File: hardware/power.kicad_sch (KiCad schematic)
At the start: 0 parts

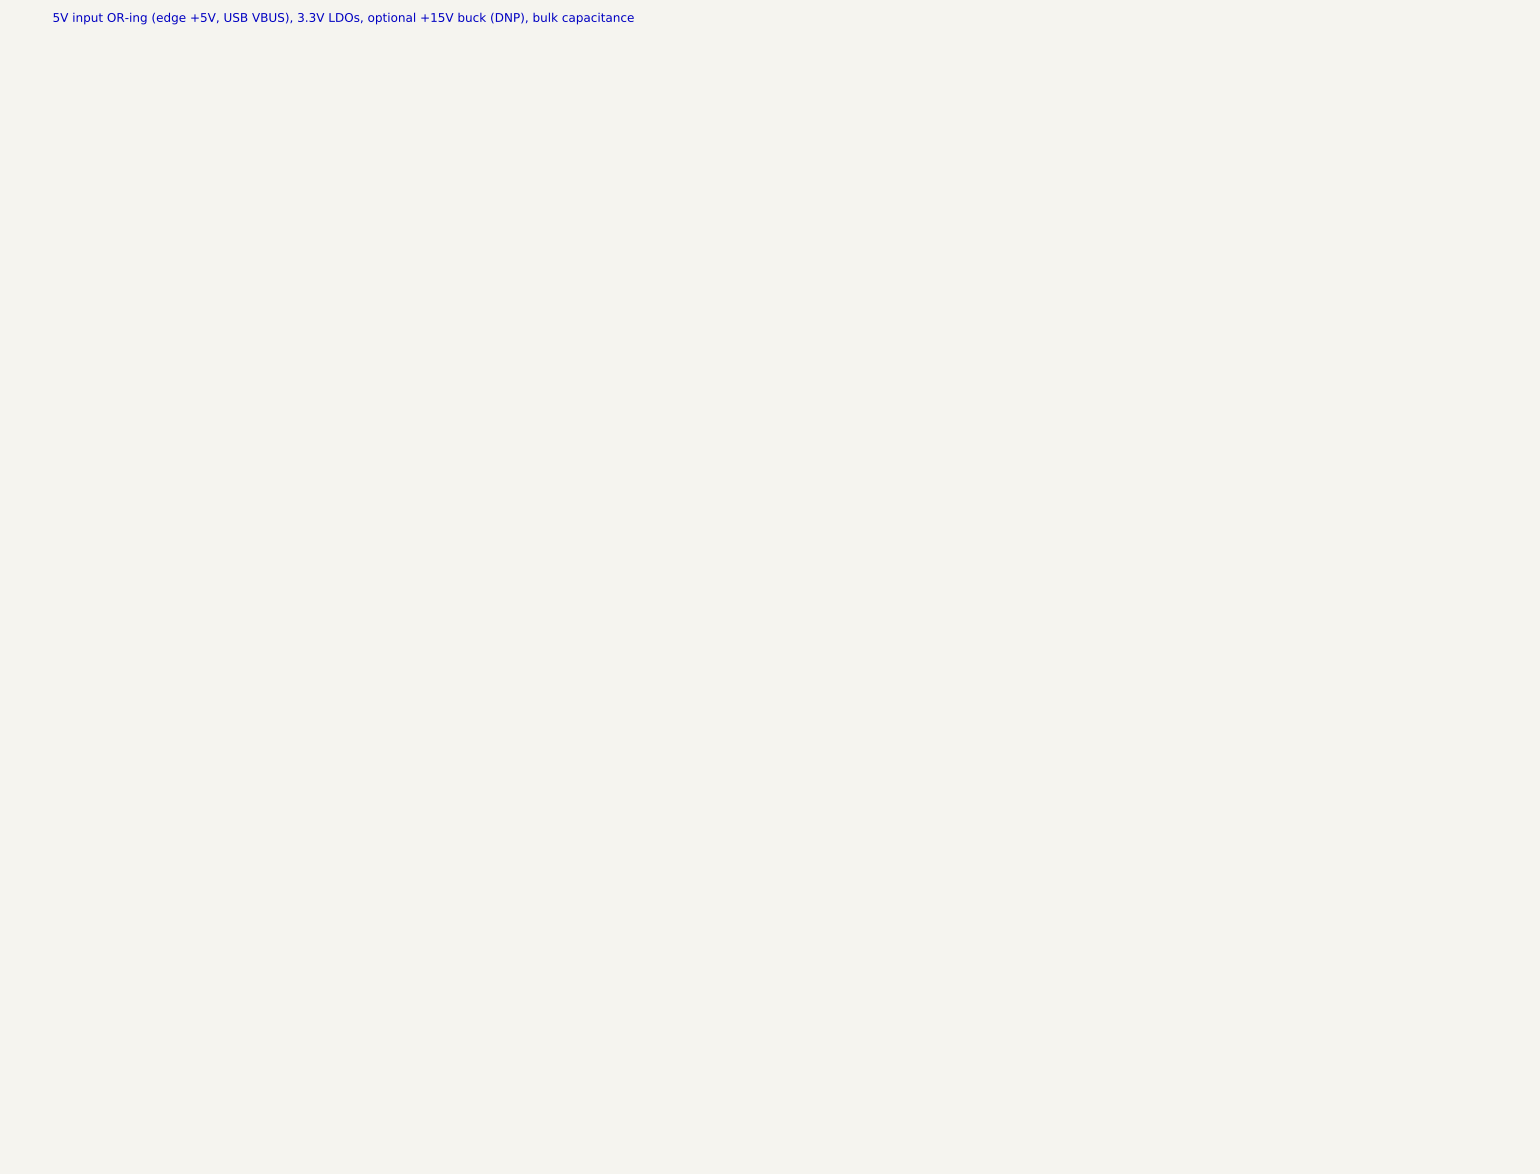
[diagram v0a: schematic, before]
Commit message: Remaining sheets: power, SD and display, WiFi, audio, joystick; ERC clean
- Power: Schottky diode-OR of edge +5V and USB VBUS (card runs from the
  2068/expansion bus, USB alone, or both), two TLV1117LV33 LDOs, bulk caps
- SD: Hirose DM3AT in SPI mode with series R, pull-ups, card detect to STAT
- OLED: 7-pin header (Waveshare 1.27in 128x96 SSD1351) on SPI1
- WiFi: ESP32-C3-WROOM-02 on UART, EN/boot from CTL, IO8 pull-up
- Audio: PWM low-pass, 2068 SOUND mix, MCP6002 buffers, 3.5 mm jack
- Joystick: DE-9 Kempston with pull-ups, series R, optional +5V jumper
- Memory sheet: activity LED on CTL bit 6
- Docs: power decision updated

Co-Authored-By: Claude Fable 5.1 <noreply@anthropic.com>
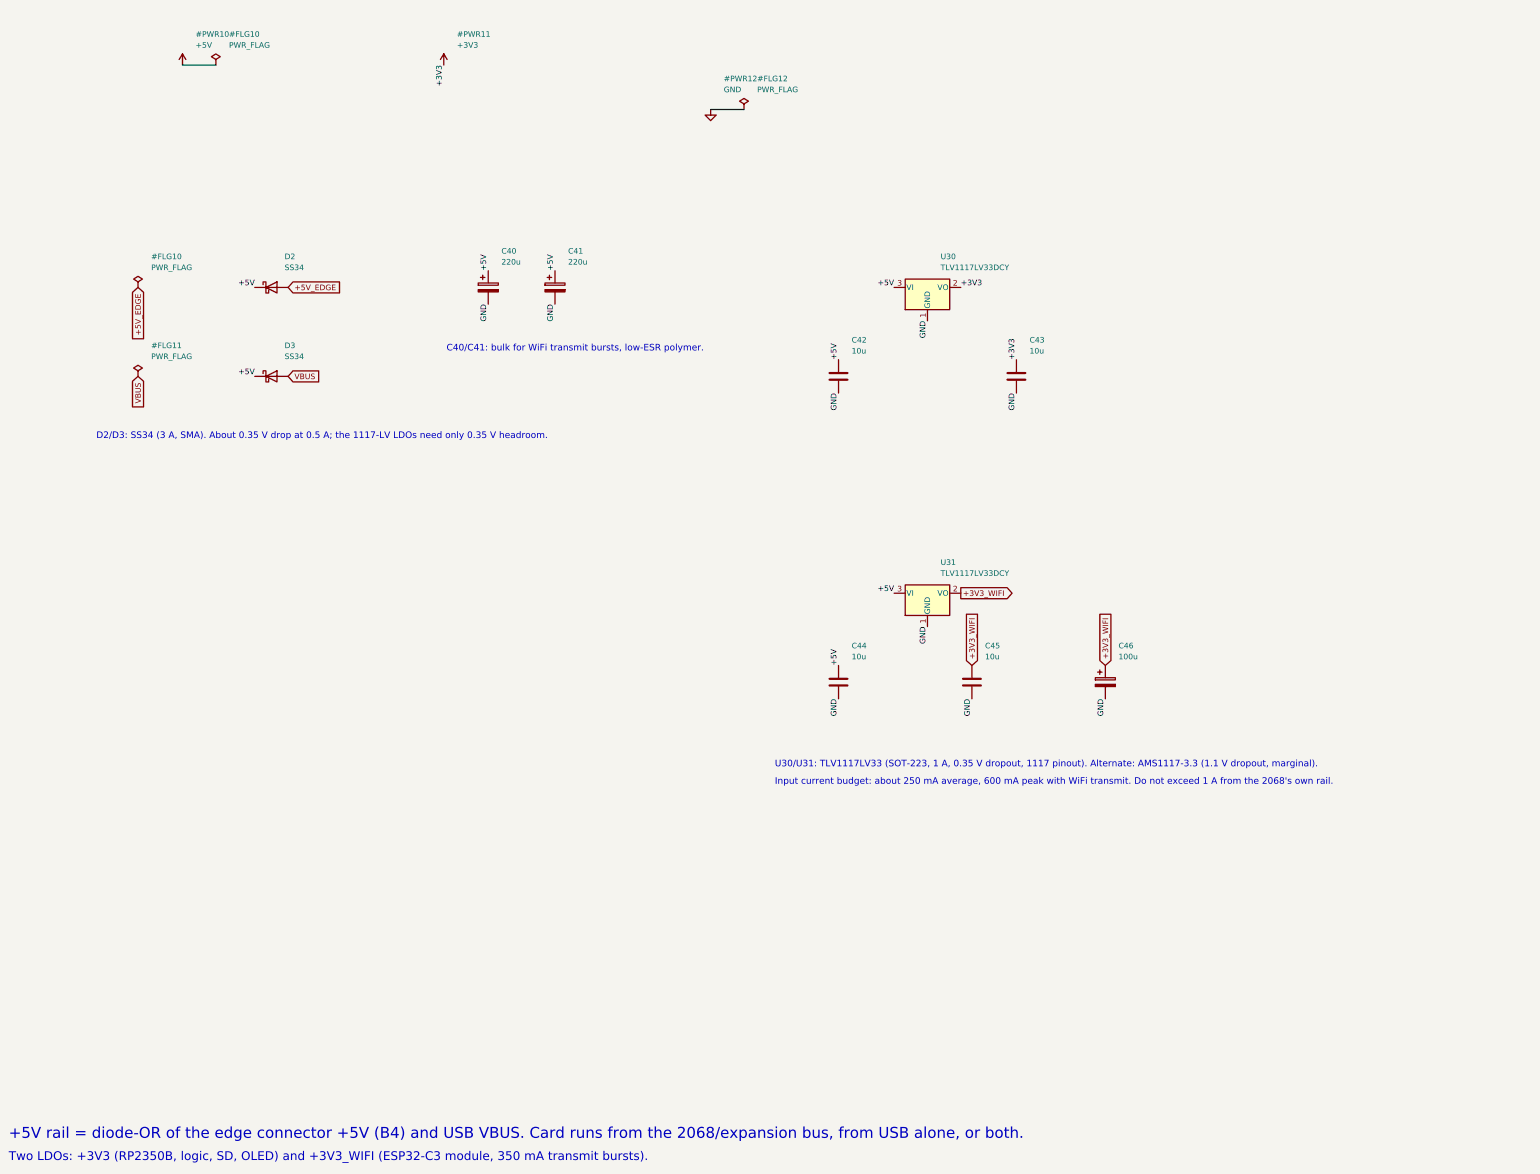
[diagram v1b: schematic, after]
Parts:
- added C40, C41: 220u, Capacitor_SMD:CP_Elec_6.3x7.7, symbol Device:C_Polarized
- added C42, C43, C44, C45: 10u, Capacitor_SMD:C_0805_2012Metric, symbol Device:C
- added C46: 100u, Capacitor_SMD:CP_Elec_6.3x7.7, symbol Device:C_Polarized
- added D2, D3: SS34, Diode_SMD:D_SMA, symbol Device:D_Schottky
- added U30, U31: TLV1117LV33DCY, Package_TO_SOT_SMD:SOT-223-3_TabPin2, symbol Regulator_Linear:TLV1117-33
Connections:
- new net +3V3: C43.1, U30.2 (VO)
- new net +3V3_WIFI: C45.1, C46.1, U31.2 (VO)
- new net +5V: C40.1, C41.1, C42.1, C44.1, D2.1 (K), D3.1 (K), U30.3 (VI), U31.3 (VI)
- new net +5V_EDGE: D2.2 (A)
- new net GND: C40.2, C41.2, C42.2, C43.2, C44.2, C45.2, C46.2, U30.1 (GND), U31.1 (GND)
- new net VBUS: D3.2 (A)
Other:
- note added: "+5V rail = diode-OR of the edge connector +5V (B4) and USB VBUS. Card runs from the 2068/expansion bus, from USB alone, or both."
- note added: "C40/C41: bulk for WiFi transmit bursts, low-ESR polymer."
- note added: "D2/D3: SS34 (3 A, SMA). About 0.35 V drop at 0.5 A; the 1117-LV LDOs need only 0.35 V headroom."
- note added: "Input current budget: about 250 mA average, 600 mA peak with WiFi transmit. Do not exceed 1 A from the 2068's own rail."
- note added: "Two LDOs: +3V3 (RP2350B, logic, SD, OLED) and +3V3_WIFI (ESP32-C3 module, 350 mA transmit bursts)."
- note added: "U30/U31: TLV1117LV33 (SOT-223, 1 A, 0.35 V dropout, 1117 pinout). Alternate: AMS1117-3.3 (1.1 V dropout, marginal)."
- note removed: "5V input OR-ing (edge +5V, USB VBUS), 3.3V LDOs, optional +15V buck (DNP), bulk capacitance"

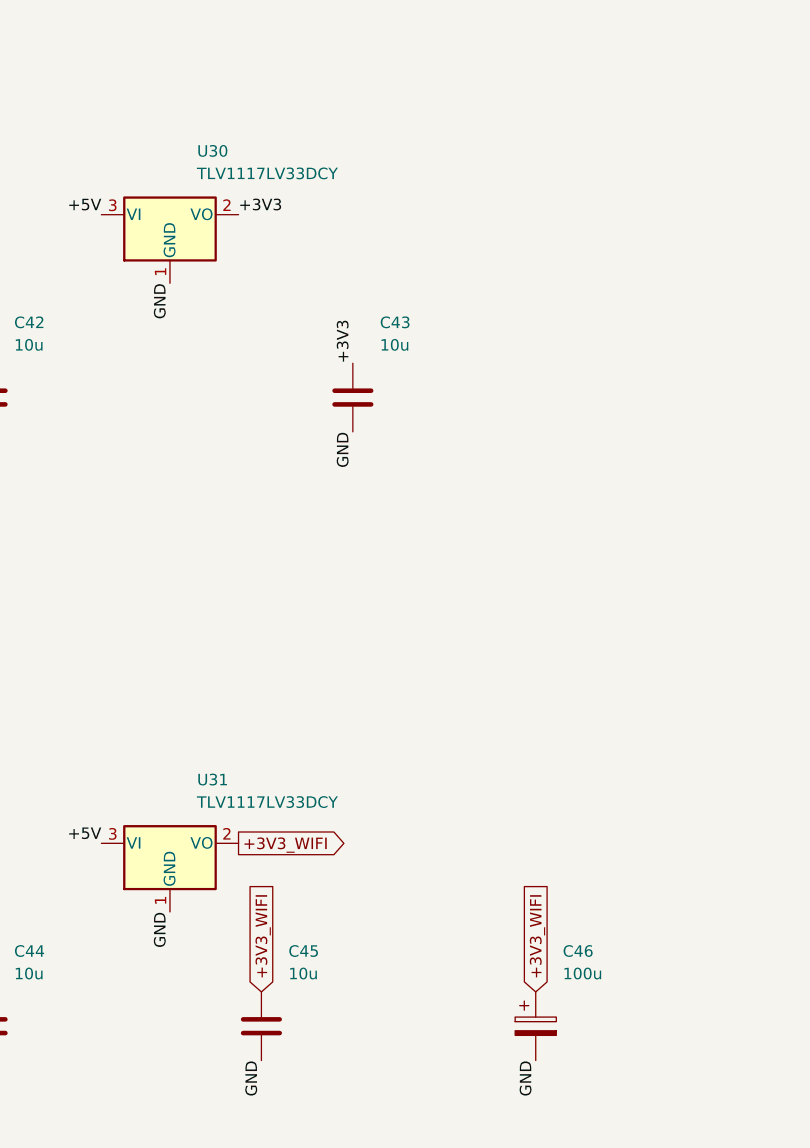
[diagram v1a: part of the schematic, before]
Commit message: BOM pass: LCSC and MPN fields on every part, JLCPCB BOM export
- scripts/parts.py: part table looked up 2026-09-16; schlib stamps fields
- substitutions for stock: 74HC273PW, 74LVC139PW, TI LVC04/08/126/574/1G86,
  33R USB series, XKB TS-1187A switches, Panasonic polymer 220uF, B5819W
- bom/: JLCPCB-format and full BOM CSVs

Co-Authored-By: Claude Fable 5.1 <noreply@anthropic.com>
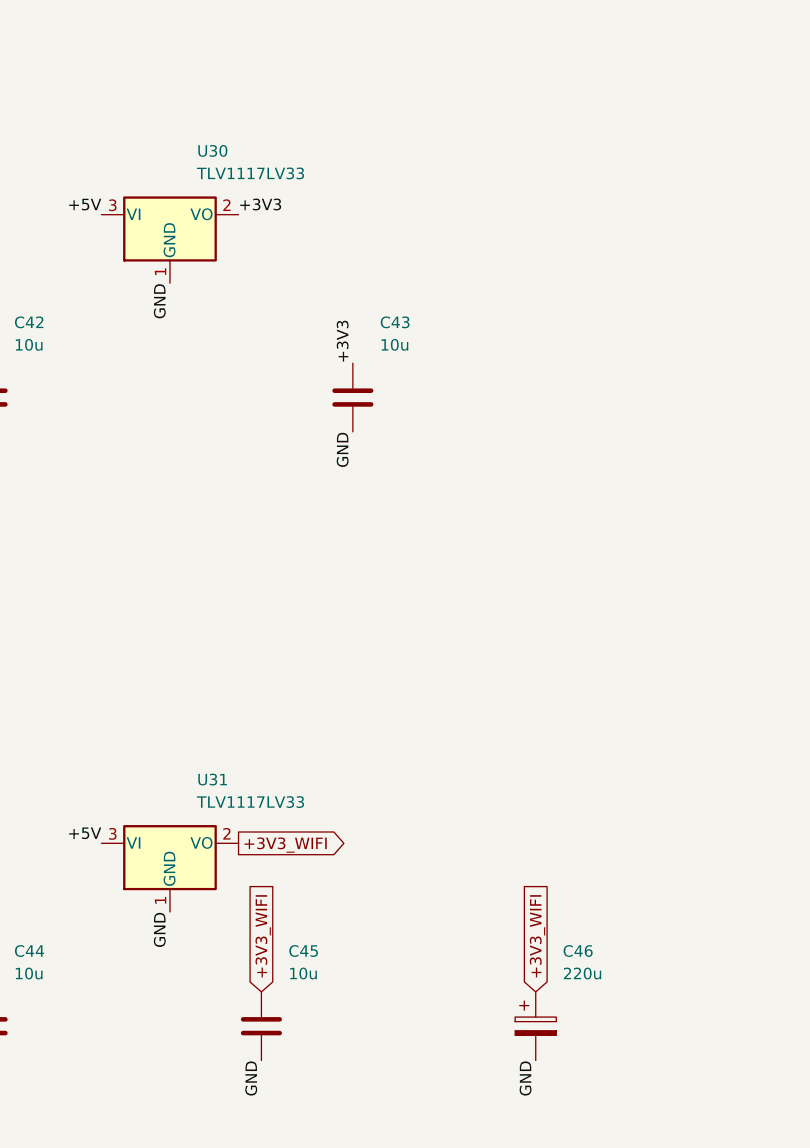
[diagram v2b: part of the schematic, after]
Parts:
- C40, C41: footprint Capacitor_SMD:CP_Elec_6.3x7.7 -> Capacitor_SMD:CP_Elec_6.3x5.9; LCSC (none) -> C128504; MPN (none) -> 6SVPC220MV
- C42, C43, C44, C45: LCSC (none) -> C15850; MPN (none) -> CL21A106KAYNNNE
- C46: value 100u -> 220u; footprint Capacitor_SMD:CP_Elec_6.3x7.7 -> Capacitor_SMD:CP_Elec_6.3x5.9; LCSC (none) -> C128504; MPN (none) -> 6SVPC220MV
- D2, D3: LCSC (none) -> C8678; MPN (none) -> SS34
- U30, U31: value TLV1117LV33DCY -> TLV1117LV33; LCSC (none) -> C15578; MPN (none) -> TLV1117LV33DCYR
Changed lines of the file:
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@@
     (property "Datasheet" "" (at 80.01 90.17 0) (effects (font (size 1.27 1.27)) (justify left) (hide yes)))
     (property "Description" "" (at 80.01 90.17 0) (effects (font (size 1.27 1.27)) (justify left) (hide yes)))
+    (property "MPN" "SS34" (at 80.01 90.17 0) (effects (font (size 1.27 1.27)) (justify left) (hide yes)))
+    (property "LCSC" "C8678" (at 80.01 90.17 0) (effects (font (size 1.27 1.27)) (justify left) (hide yes)))
     (pin "1")
     (pin "2")
@@
     (property "Datasheet" "" (at 80.01 110.49 0) (effects (font (size 1.27 1.27)) (justify left) (hide yes)))
     (property "Description" "" (at 80.01 110.49 0) (effects (font (size 1.27 1.27)) (justify left) (hide yes)))
+    (property "MPN" "SS34" (at 80.01 110.49 0) (effects (font (size 1.27 1.27)) (justify left) (hide yes)))
+    (property "LCSC" "C8678" (at 80.01 110.49 0) (effects (font (size 1.27 1.27)) (justify left) (hide yes)))
     (pin "1")
     (pin "2")
@@
     (property "Reference" "C40" (at 132.54 81.86 0) (effects (font (size 1.27 1.27)) (justify left)))
     (property "Value" "220u" (at 132.54 84.36 0) (effects (font (size 1.27 1.27)) (justify left)))
-    (property "Footprint" "Capacitor_SMD:CP_Elec_6.3x7.7" (at 129.54 90.17 0) (effects (font (size 1.27 1.27)) (justify left) (hide yes)))
+    (property "Footprint" "Capacitor_SMD:CP_Elec_6.3x5.9" (at 129.54 90.17 0) (effects (font (size 1.27 1.27)) (justify left) (hide yes)))
     (property "Datasheet" "" (at 129.54 90.17 0) (effects (font (size 1.27 1.27)) (justify left) (hide yes)))
     (property "Description" "" (at 129.54 90.17 0) (effects (font (size 1.27 1.27)) (justify left) (hide yes)))
+    (property "MPN" "6SVPC220MV" (at 129.54 90.17 0) (effects (font (size 1.27 1.27)) (justify left) (hide yes)))
+    (property "LCSC" "C128504" (at 129.54 90.17 0) (effects (font (size 1.27 1.27)) (justify left) (hide yes)))
     (pin "1")
     (pin "2")
@@
     (property "Reference" "C41" (at 147.78 81.86 0) (effects (font (size 1.27 1.27)) (justify left)))
     (property "Value" "220u" (at 147.78 84.36 0) (effects (font (size 1.27 1.27)) (justify left)))
-    (property "Footprint" "Capacitor_SMD:CP_Elec_6.3x7.7" (at 144.78 90.17 0) (effects (font (size 1.27 1.27)) (justify left) (hide yes)))
+    (property "Footprint" "Capacitor_SMD:CP_Elec_6.3x5.9" (at 144.78 90.17 0) (effects (font (size 1.27 1.27)) (justify left) (hide yes)))
     (property "Datasheet" "" (at 144.78 90.17 0) (effects (font (size 1.27 1.27)) (justify left) (hide yes)))
     (property "Description" "" (at 144.78 90.17 0) (effects (font (size 1.27 1.27)) (justify left) (hide yes)))
+    (property "MPN" "6SVPC220MV" (at 144.78 90.17 0) (effects (font (size 1.27 1.27)) (justify left) (hide yes)))
+    (property "LCSC" "C128504" (at 144.78 90.17 0) (effects (font (size 1.27 1.27)) (justify left) (hide yes)))
     (pin "1")
     (pin "2")
@@
     (exclude_from_sim no) (in_bom yes) (on_board yes) (dnp no)
     (property "Reference" "U30" (at 232.87 83.13 0) (effects (font (size 1.27 1.27)) (justify left)))
-    (property "Value" "TLV1117LV33DCY" (at 232.87 85.63 0) (effects (font (size 1.27 1.27)) (justify left)))
+    (property "Value" "TLV1117LV33" (at 232.87 85.63 0) (effects (font (size 1.27 1.27)) (justify left)))
     (property "Footprint" "Package_TO_SOT_SMD:SOT-223-3_TabPin2" (at 229.87 90.17 0) (effects (font (size 1.27 1.27)) (justify left) (hide yes)))
     (property "Datasheet" "" (at 229.87 90.17 0) (effects (font (size 1.27 1.27)) (justify left) (hide yes)))
     (property "Description" "" (at 229.87 90.17 0) (effects (font (size 1.27 1.27)) (justify left) (hide yes)))
+    (property "MPN" "TLV1117LV33DCYR" (at 229.87 90.17 0) (effects (font (size 1.27 1.27)) (justify left) (hide yes)))
+    (property "LCSC" "C15578" (at 229.87 90.17 0) (effects (font (size 1.27 1.27)) (justify left) (hide yes)))
     (pin "1")
     (pin "2")
@@
     (property "Datasheet" "" (at 209.55 110.49 0) (effects (font (size 1.27 1.27)) (justify left) (hide yes)))
     (property "Description" "" (at 209.55 110.49 0) (effects (font (size 1.27 1.27)) (justify left) (hide yes)))
+    (property "MPN" "CL21A106KAYNNNE" (at 209.55 110.49 0) (effects (font (size 1.27 1.27)) (justify left) (hide yes)))
+    (property "LCSC" "C15850" (at 209.55 110.49 0) (effects (font (size 1.27 1.27)) (justify left) (hide yes)))
     (pin "1")
     (pin "2")
@@
     (property "Datasheet" "" (at 250.19 110.49 0) (effects (font (size 1.27 1.27)) (justify left) (hide yes)))
     (property "Description" "" (at 250.19 110.49 0) (effects (font (size 1.27 1.27)) (justify left) (hide yes)))
+    (property "MPN" "CL21A106KAYNNNE" (at 250.19 110.49 0) (effects (font (size 1.27 1.27)) (justify left) (hide yes)))
+    (property "LCSC" "C15850" (at 250.19 110.49 0) (effects (font (size 1.27 1.27)) (justify left) (hide yes)))
     (pin "1")
     (pin "2")
@@
     (exclude_from_sim no) (in_bom yes) (on_board yes) (dnp no)
     (property "Reference" "U31" (at 232.87 152.98 0) (effects (font (size 1.27 1.27)) (justify left)))
-    (property "Value" "TLV1117LV33DCY" (at 232.87 155.48 0) (effects (font (size 1.27 1.27)) (justify left)))
+    (property "Value" "TLV1117LV33" (at 232.87 155.48 0) (effects (font (size 1.27 1.27)) (justify left)))
     (property "Footprint" "Package_TO_SOT_SMD:SOT-223-3_TabPin2" (at 229.87 160.02 0) (effects (font (size 1.27 1.27)) (justify left) (hide yes)))
     (property "Datasheet" "" (at 229.87 160.02 0) (effects (font (size 1.27 1.27)) (justify left) (hide yes)))
     (property "Description" "" (at 229.87 160.02 0) (effects (font (size 1.27 1.27)) (justify left) (hide yes)))
+    (property "MPN" "TLV1117LV33DCYR" (at 229.87 160.02 0) (effects (font (size 1.27 1.27)) (justify left) (hide yes)))
+    (property "LCSC" "C15578" (at 229.87 160.02 0) (effects (font (size 1.27 1.27)) (justify left) (hide yes)))
     (pin "1")
     (pin "2")
@@
     (property "Datasheet" "" (at 209.55 180.34 0) (effects (font (size 1.27 1.27)) (justify left) (hide yes)))
     (property "Description" "" (at 209.55 180.34 0) (effects (font (size 1.27 1.27)) (justify left) (hide yes)))
+    (property "MPN" "CL21A106KAYNNNE" (at 209.55 180.34 0) (effects (font (size 1.27 1.27)) (justify left) (hide yes)))
+    (property "LCSC" "C15850" (at 209.55 180.34 0) (effects (font (size 1.27 1.27)) (justify left) (hide yes)))
     (pin "1")
     (pin "2")
@@
     (property "Datasheet" "" (at 240.03 180.34 0) (effects (font (size 1.27 1.27)) (justify left) (hide yes)))
     (property "Description" "" (at 240.03 180.34 0) (effects (font (size 1.27 1.27)) (justify left) (hide yes)))
+    (property "MPN" "CL21A106KAYNNNE" (at 240.03 180.34 0) (effects (font (size 1.27 1.27)) (justify left) (hide yes)))
+    (property "LCSC" "C15850" (at 240.03 180.34 0) (effects (font (size 1.27 1.27)) (justify left) (hide yes)))
     (pin "1")
     (pin "2")
@@
     (exclude_from_sim no) (in_bom yes) (on_board yes) (dnp no)
     (property "Reference" "C46" (at 273.51 172.03 0) (effects (font (size 1.27 1.27)) (justify left)))
-    (property "Value" "100u" (at 273.51 174.53 0) (effects (font (size 1.27 1.27)) (justify left)))
-    (property "Footprint" "Capacitor_SMD:CP_Elec_6.3x7.7" (at 270.51 180.34 0) (effects (font (size 1.27 1.27)) (justify left) (hide yes)))
+    (property "Value" "220u" (at 273.51 174.53 0) (effects (font (size 1.27 1.27)) (justify left)))
+    (property "Footprint" "Capacitor_SMD:CP_Elec_6.3x5.9" (at 270.51 180.34 0) (effects (font (size 1.27 1.27)) (justify left) (hide yes)))
     (property "Datasheet" "" (at 270.51 180.34 0) (effects (font (size 1.27 1.27)) (justify left) (hide yes)))
     (property "Description" "" (at 270.51 180.34 0) (effects (font (size 1.27 1.27)) (justify left) (hide yes)))
+    (property "MPN" "6SVPC220MV" (at 270.51 180.34 0) (effects (font (size 1.27 1.27)) (justify left) (hide yes)))
+    (property "LCSC" "C128504" (at 270.51 180.34 0) (effects (font (size 1.27 1.27)) (justify left) (hide yes)))
     (pin "1")
     (pin "2")
